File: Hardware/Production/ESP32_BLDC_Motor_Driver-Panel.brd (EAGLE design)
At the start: 198.4 x 136.1 mm, 742 parts, among them J1 USB-C Connector, J11 USB-C Connector, J12 Breadboard Connector, J13 Breadboard Headers, J14 QWIIC_RIGHT_ANGLE, J16 USB-C Connector, J17 Breadboard Connector, J18 Breadboard Headers, J19 QWIIC_RIGHT_ANGLE, J3 USB-C Connector, J4 Breadboard Connector, J5 Breadboard Headers, J6 Breadboard Connector, J7 QWIIC_RIGHT_ANGLE, J8 Breadboard Headers, J9 QWIIC_RIGHT_ANGLE, P1 0532610371, P2 0532610371, P3 0532610371, P4 0532610371, Q10 NPN Transistors, Q12 20V/4.2A/52mΩ/1.4W, Q2 NPN Transistors, Q3 20V/4.2A/52mΩ/1.4W, Q4 NPN Transistors, Q6 20V/4.2A/52mΩ/1.4W, Q7 NPN Transistors, Q9 20V/4.2A/52mΩ/1.4W, U1 TMC6300, U10 INA240A1, U11 INA240A1, U12 TMC6300, U13 ESP-WROOM-3232D, U14 CH340C, U15 ESD Diode, U16 TMAG5273, U17 3.3V, U18 AP63357, U19 INA240A1, U2 3.3V, U20 INA240A1, U21 INA240A1, U22 OPA344, U23 TMC6300, U24 ESP-WROOM-3232D, U25 CH340C, U26 ESD Diode, U27 TMAG5273, U28 3.3V, U29 AP63357, U3 ESP-WROOM-3232D, U30 INA240A1, U31 INA240A1, U32 INA240A1, U33 OPA344, U34 TMC6300, U35 ESP-WROOM-3232D, U36 CH340C, U37 ESD Diode, U38 TMAG5273, U39 3.3V, U4 CH340C, U40 AP63357, U41 INA240A1, U42 INA240A1, U43 INA240A1, U44 OPA344, U5 ESD Diode, U6 AP63357, U7 INA240A1, U8 TMAG5273, U9 OPA344

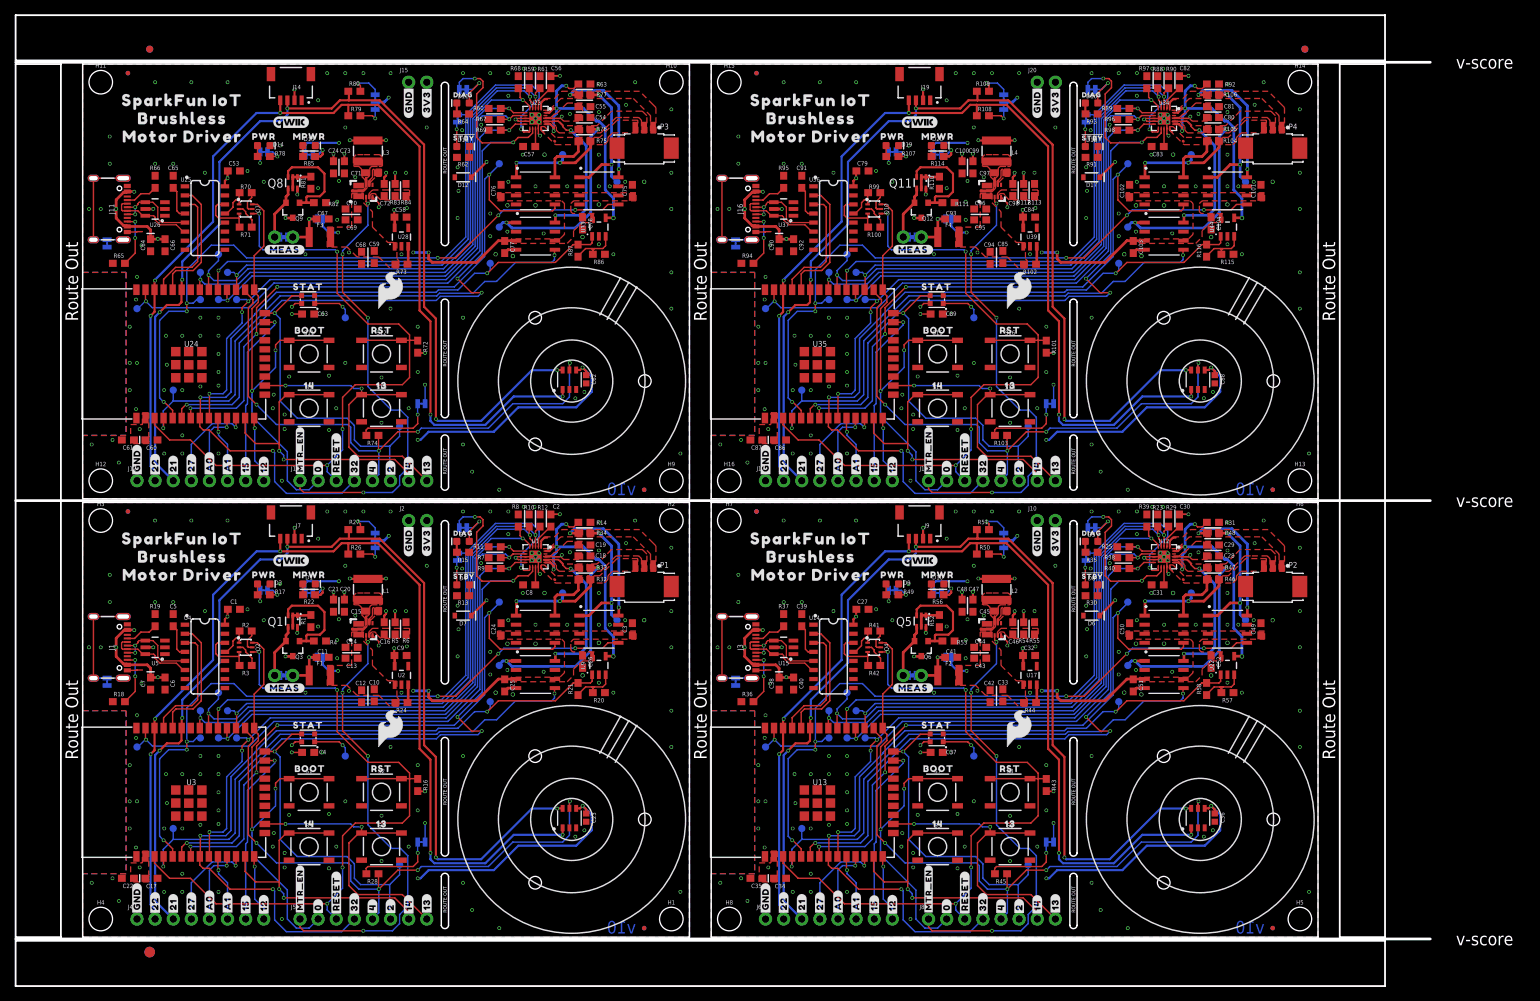
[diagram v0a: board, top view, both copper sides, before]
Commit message: Updated files for ordering
Completed all the final requests from the re-review after the reds review; double checked the test points to the test board; updated pcb spacers; updated files for ordering boards
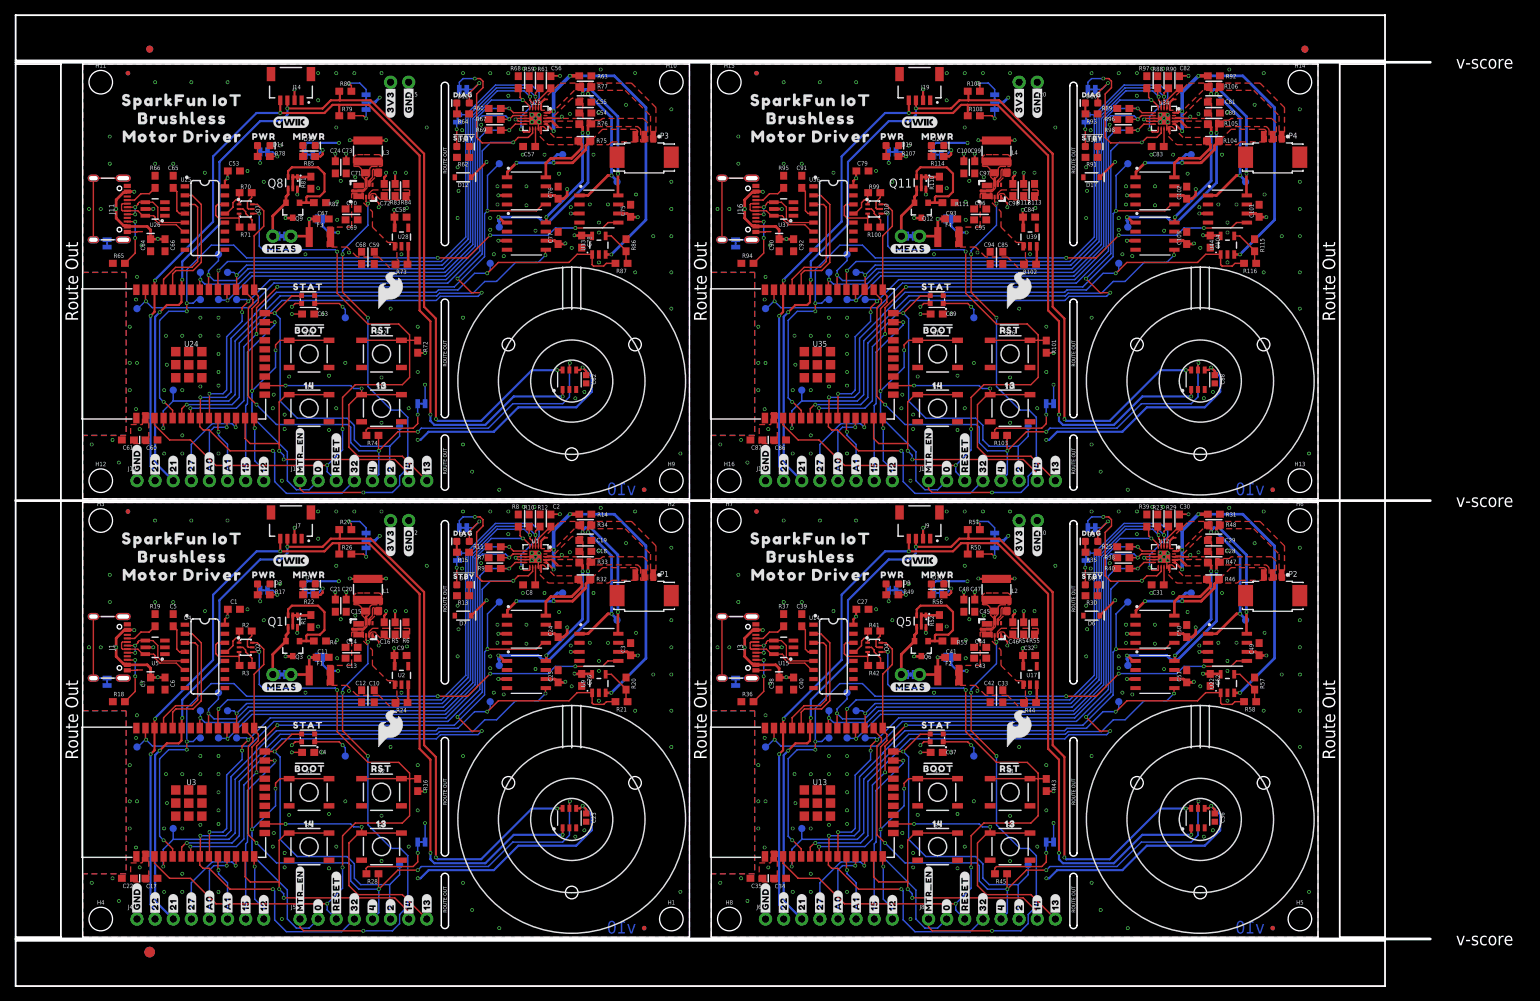
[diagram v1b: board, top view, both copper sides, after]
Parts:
- added U$245: (no value), output:#DIAG#15
- added U$246: (no value), output:##STBY##16
- added U$247, U$251: (no value), output:#GND#17
- added U$248, U$250: (no value), output:#3V3#18
- added U$249: (no value), output:#2#RGB#18
- added U$252: (no value), output:#0##BOOT##0
- U$123, U$59: device SparkFun-Aesthetics:ORDERING_INSTRUCTIONS -> output:#2#RGB#18
- U$124, U$185: device output:#I2C#630063003467 -> output:#3V3#18
- U$125: device output:#SHLD#630063003467 -> output:#GND#17
- U$126: device output:##INT#630063003473 -> output:#0##BOOT##0
- U$127: device SparkFun-Aesthetics:SFE_LOGO_NAME_FLAME_.2 -> SparkFun-Aesthetics:ORDERING_INSTRUCTIONS
- U$128: device output:MOTOR_DRIVER630063003515 -> output:#I2C#630063003467
- U$129: device OT-EM3215:OT-EM3215 -> output:#SHLD#630063003467
- U$130: device output:STAT1630063003522 -> output:##INT#630063003473
- U$131: device output:RST1630063003525 -> SparkFun-Aesthetics:SFE_LOGO_NAME_FLAME_.2
- U$132: device output:BOOT21630063003532 -> output:MOTOR_DRIVER630063003515
- U$133: device output:PWR21630063003533 -> OT-EM3215:OT-EM3215
- U$134: device output:#2#LED#21630063003534 -> output:STAT1630063003522
- U$135: device output:#4#INT_MAG#21630063003534 -> output:RST1630063003525
- U$136: device output:#32#CURR_SENSE#10 -> output:BOOT21630063003532
- U$137: device output:#PWR#33 -> output:PWR21630063003533
- U$138: device output:#RESET#34 -> output:#4#INT_MAG#21630063003534
- U$139: device output:#RESET#34 -> output:#32#CURR_SENSE#10
- U$140: device output:#0#QWR#36 -> output:#PWR#33
- U$141: device output:#12#GPIO1#4 -> output:#RESET#34
- U$142: device output:#15#GPIO4#13 -> output:#RESET#34
- U$143: device output:#27#GPIO2#27 -> output:#12#GPIO1#4
- U$144: device output:#21#SDA#29 -> output:#15#GPIO4#13
- U$145: device output:#22#SCL#30 -> output:#27#GPIO2#27
- U$146: device output:#A0#30 -> output:#21#SDA#29
- U$147: device output:#26#A0#30 -> output:#22#SCL#30
- U$148: device output:#25#A1#30 -> output:#A0#30
- U$149: device output:#A1#30 -> output:#26#A0#30
- U$150: device output:#12#31 -> output:#25#A1#30
- U$151: device output:#GND#32 -> output:#A1#30
- U$152: device output:#GND#32 -> output:#12#31
- U$153: device output:#22#33 -> output:#GND#32
- U$154: device output:#21#33 -> output:#GND#32
- U$155: device output:#27#33 -> output:#22#33
- U$156: device output:#15#33 -> output:#21#33
- U$157: device output:#0#33 -> output:#27#33
- U$158: device output:#32#33 -> output:#15#33
- U$159: device output:#4#33 -> output:#0#33
- U$16: device output:#2#LED#21630063003534 -> output:#3V3#18
- U$160: device output:#2#33 -> output:#32#33
- U$161: device output:#14#AUX1#36 -> output:#4#33
- U$162: device output:#14#36 -> output:#2#33
- U$163: device output:#13#36 -> output:#14#AUX1#36
- U$164: device output:1436 -> output:#14#36
- U$165: device output:131437 -> output:#13#36
- U$166: device output:#BYP#131439 -> output:1436
- U$167: device output:SPARKFUN_IOT131442 -> output:131437
- U$168: device output:BRUSHLESS131445 -> output:#BYP#131439
- U$169: device output:MOTOR_DRIVER131446 -> output:SPARKFUN_IOT131442
- U$170: device output:MPWR131449 -> output:BRUSHLESS131445
- U$171: device output:#MEAS#131453 -> output:MOTOR_DRIVER131446
- U$172: device output:#MEAS#131453 -> output:MPWR131449
- U$173: device output:IOT_BRUSHLESS131454 -> output:#MEAS#131453
- U$174: device output:#MTR_EN#131458 -> output:#MEAS#131453
- U$175: device output:#MTR_EN#131460 -> output:IOT_BRUSHLESS131454
- U$176: device output:#MPWR#131468 -> output:#MTR_EN#131458
- U$177: device output:DIAG131469 -> output:#MTR_EN#131460
- U$178: device output:#STBY#131470 -> output:#MPWR#131468
- U$179: device output:#13#AUX2#14 -> output:DIAG131469
- U$180: device output:#DIAG#15 -> output:#STBY#131470
- U$181: device output:##STBY##16 -> output:#13#AUX2#14
- U$182: device output:#GND#17 -> output:#DIAG#15
- U$183: device output:#3V3#18 -> output:##STBY##16
- U$184: device SparkFun-Aesthetics:ORDERING_INSTRUCTIONS -> output:#GND#17
- U$186: device output:#SHLD#630063003467 -> output:#2#RGB#18
- U$187: device output:##INT#630063003473 -> output:#3V3#18
- U$188: device SparkFun-Aesthetics:SFE_LOGO_NAME_FLAME_.2 -> output:#GND#17
- U$189: device output:MOTOR_DRIVER630063003515 -> output:#0##BOOT##0
- U$190: device OT-EM3215:OT-EM3215 -> SparkFun-Aesthetics:ORDERING_INSTRUCTIONS
- U$191: device output:STAT1630063003522 -> output:#I2C#630063003467
- U$192: device output:RST1630063003525 -> output:#SHLD#630063003467
- U$193: device output:BOOT21630063003532 -> output:##INT#630063003473
- U$194: device output:PWR21630063003533 -> SparkFun-Aesthetics:SFE_LOGO_NAME_FLAME_.2
- U$195: device output:#2#LED#21630063003534 -> output:MOTOR_DRIVER630063003515
- U$196: device output:#4#INT_MAG#21630063003534 -> OT-EM3215:OT-EM3215
- U$197: device output:#32#CURR_SENSE#10 -> output:STAT1630063003522
- U$198: device output:#PWR#33 -> output:RST1630063003525
- U$199: device output:#RESET#34 -> output:BOOT21630063003532
- U$200: device output:#RESET#34 -> output:PWR21630063003533
- U$201: device output:#0#QWR#36 -> output:#4#INT_MAG#21630063003534
- U$202: device output:#12#GPIO1#4 -> output:#32#CURR_SENSE#10
- U$203: device output:#15#GPIO4#13 -> output:#PWR#33
- U$204: device output:#27#GPIO2#27 -> output:#RESET#34
- U$205: device output:#21#SDA#29 -> output:#RESET#34
- U$206: device output:#22#SCL#30 -> output:#12#GPIO1#4
- U$207: device output:#A0#30 -> output:#15#GPIO4#13
- U$208: device output:#26#A0#30 -> output:#27#GPIO2#27
- U$209: device output:#25#A1#30 -> output:#21#SDA#29
- U$210: device output:#A1#30 -> output:#22#SCL#30
- U$211: device output:#12#31 -> output:#A0#30
- U$212: device output:#GND#32 -> output:#26#A0#30
- U$213: device output:#GND#32 -> output:#25#A1#30
- U$214: device output:#22#33 -> output:#A1#30
- U$215: device output:#21#33 -> output:#12#31
- U$216: device output:#27#33 -> output:#GND#32
- U$217: device output:#15#33 -> output:#GND#32
- U$218: device output:#0#33 -> output:#22#33
- U$219: device output:#32#33 -> output:#21#33
- U$220: device output:#4#33 -> output:#27#33
- U$221: device output:#2#33 -> output:#15#33
- U$222: device output:#14#AUX1#36 -> output:#0#33
- U$223: device output:#14#36 -> output:#32#33
- U$224: device output:#13#36 -> output:#4#33
- U$225: device output:1436 -> output:#2#33
- U$226: device output:131437 -> output:#14#AUX1#36
- U$227: device output:#BYP#131439 -> output:#14#36
- U$228: device output:SPARKFUN_IOT131442 -> output:#13#36
- U$229: device output:BRUSHLESS131445 -> output:1436
- U$230: device output:MOTOR_DRIVER131446 -> output:131437
- U$231: device output:MPWR131449 -> output:#BYP#131439
- U$232: device output:#MEAS#131453 -> output:SPARKFUN_IOT131442
- U$233: device output:#MEAS#131453 -> output:BRUSHLESS131445
- U$234: device output:IOT_BRUSHLESS131454 -> output:MOTOR_DRIVER131446
- U$235: device output:#MTR_EN#131458 -> output:MPWR131449
- U$236: device output:#MTR_EN#131460 -> output:#MEAS#131453
- U$237: device output:#MPWR#131468 -> output:#MEAS#131453
- U$238: device output:DIAG131469 -> output:IOT_BRUSHLESS131454
- U$239: device output:#STBY#131470 -> output:#MTR_EN#131458
- U$240: device output:#13#AUX2#14 -> output:#MTR_EN#131460
- U$241: device output:#DIAG#15 -> output:#MPWR#131468
- U$242: device output:##STBY##16 -> output:DIAG131469
- U$243: device output:#GND#17 -> output:#STBY#131470
- U$244: device output:#3V3#18 -> output:#13#AUX2#14
- U$32: device output:#0#QWR#36 -> output:#0##BOOT##0
- U$60: device output:#I2C#630063003467 -> output:#GND#17
- U$61: device output:#SHLD#630063003467 -> SparkFun-Aesthetics:ORDERING_INSTRUCTIONS
- U$65: device output:##INT#630063003473 -> output:#I2C#630063003467
- U$66: device SparkFun-Aesthetics:SFE_LOGO_NAME_FLAME_.2 -> output:#SHLD#630063003467
- U$67: device output:MOTOR_DRIVER630063003515 -> output:##INT#630063003473
- U$68: device OT-EM3215:OT-EM3215 -> SparkFun-Aesthetics:SFE_LOGO_NAME_FLAME_.2
- U$69: device output:STAT1630063003522 -> output:MOTOR_DRIVER630063003515
- U$70: device output:RST1630063003525 -> OT-EM3215:OT-EM3215
- U$71: device output:BOOT21630063003532 -> output:STAT1630063003522
- U$72: device output:PWR21630063003533 -> output:RST1630063003525
- U$73: device output:#2#LED#21630063003534 -> output:BOOT21630063003532
- U$74: device output:#4#INT_MAG#21630063003534 -> output:PWR21630063003533
- U$75: device output:#32#CURR_SENSE#10 -> output:#4#INT_MAG#21630063003534
- U$76: device output:#PWR#33 -> output:#32#CURR_SENSE#10
- U$77: device output:#RESET#34 -> output:#PWR#33
- U$79: device output:#0#QWR#36 -> output:#RESET#34
- moved U$59 155.6 mm to (43.2, 6.10), flipped to the bottom, turned to 90 degrees
- moved U$184 145.3 mm to (45.7, 117.1), turned to 90 degrees
- moved U$125 136.5 mm to (133.9, 55.6), turned to 90 degrees
- moved U$189 125.5 mm to (33.0, 68.2), turned to 90 degrees
- moved U$123 113.6 mm to (131.3, 6.10), flipped to the bottom, turned to 90 degrees
- moved U$124 110.7 mm to (131.3, 55.6), turned to 90 degrees
- moved U$61 101.7 mm to (191.0, 54.6), flipped to the top
- moved U$126 101.4 mm to (121.2, 6.73), turned to 90 degrees
- moved U$187 101.0 mm to (43.2, 117.1), turned to 90 degrees
- moved U$185 85.9 mm to (43.2, 117.1), flipped to the top, turned to 90 degrees
- moved U$188 83.5 mm to (45.7, 117.1), turned to 90 degrees
- moved U$60 83.3 mm to (45.7, 55.6), turned to 90 degrees
- moved U$127 70.8 mm to (102.9, 116.1), flipped to the top
- moved U$129 67.6 mm to (3.30, 95.4), flipped to the bottom, turned to 0 degrees
- moved U$228 61.7 mm to (136.4, 66.0), turned to 90 degrees
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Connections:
- removed net N$41 (its old number): R57.2, R58.1, U22.3
- removed net N$62 (its old number): R86.2, R87.1, U33.3
- removed net N$83: R115.2, R116.1, U44.3
- new net N$40: R57.2, R58.1, U22.4
- new net N$60: R86.2, R87.1, U33.4
- new net N$80: R115.2, R116.1, U44.4
- net N$14: now also U9.4; no longer U9.3
- net SENSE: now also U9.3; no longer U9.4
- net SENSE1: now also U22.3; no longer U22.4
- net SENSE2: now also U33.3; no longer U33.4
- net SENSE3: now also U44.3; no longer U44.4
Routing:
- net SENSE2: track 35.4 -> 48.7 mm
- net SENSE: track 35.4 -> 48.7 mm
- net SENSE3: track 35.4 -> 48.7 mm
- net SENSE1: track 35.4 -> 48.7 mm
- net N$62 (its old number): track 7.20 -> 0.00 mm
- net N$41 (its old number): track 7.20 -> 0.00 mm
- net N$83: track 7.20 -> 0.00 mm
- net N$60: track 0.00 -> 5.58 mm
- net N$80: track 0.00 -> 5.58 mm
- net N$40: track 0.00 -> 5.58 mm
- net ESP_35/U_OUT3: track 86.0 -> 80.5 mm
- net ESP_35/U_OUT1: track 86.0 -> 80.5 mm
- net ESP_35/U_OUT2: track 86.0 -> 80.5 mm
- net ESP_35/U_OUT: track 86.0 -> 80.5 mm
- net SENSE_V3: track 21.8 -> 18.3 mm
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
